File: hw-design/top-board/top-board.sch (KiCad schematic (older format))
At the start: 0 parts

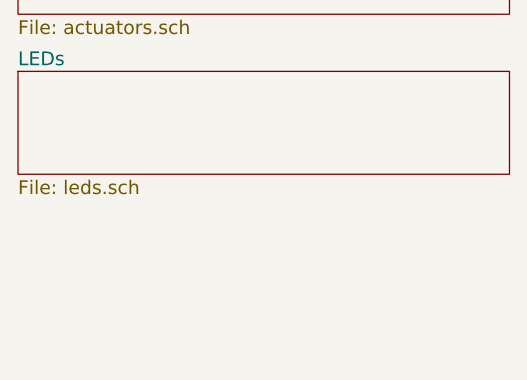
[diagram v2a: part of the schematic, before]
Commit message: top-board: fiducial and holes added to schematic
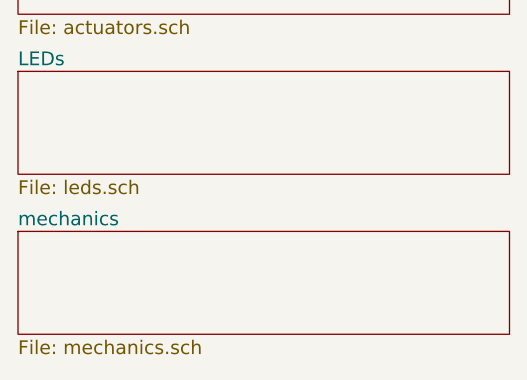
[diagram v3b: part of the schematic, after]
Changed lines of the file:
@@
 $Descr A4 11693 8268
 encoding utf-8
-Sheet 1 6
+Sheet 1 7
 Title "MOD Duo - Top Board"
 Date ""
@@
 F1 "leds.sch" 60
 $EndSheet
+$Sheet
+S 1000 4300 2150 450
+U 55F842EE
+F0 "mechanics" 60
+F1 "mechanics.sch" 60
+$EndSheet
 $EndSCHEMATC
